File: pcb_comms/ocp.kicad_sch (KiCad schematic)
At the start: 10 parts, among them IC1 LDL1117S33R, IC2 TPS2553QDBVRQ1

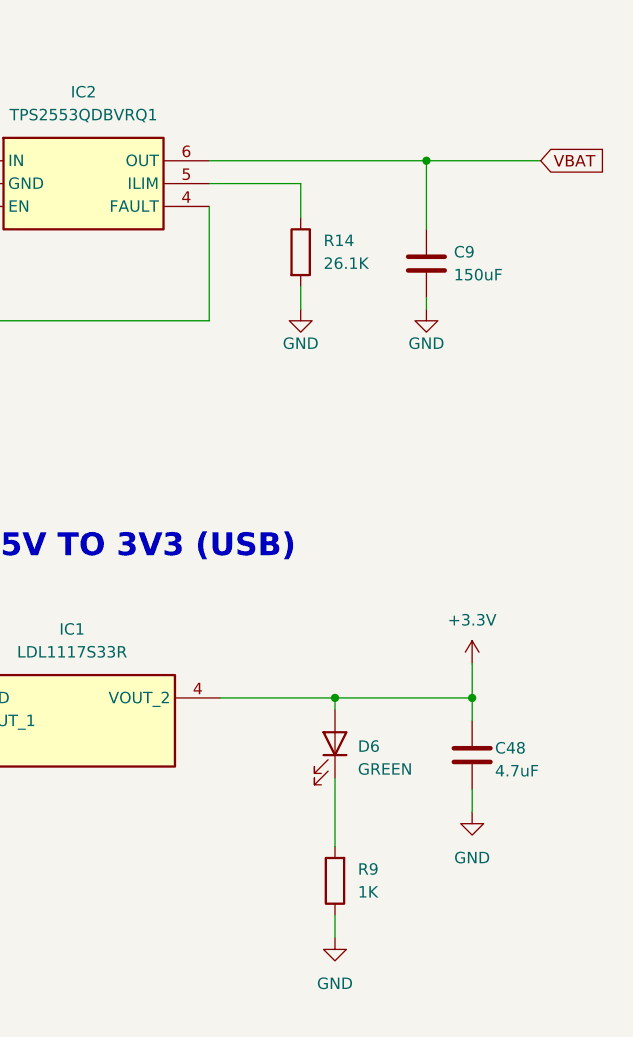
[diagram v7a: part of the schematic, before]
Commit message: Update schematic. Add net classes and JST footprints for aux
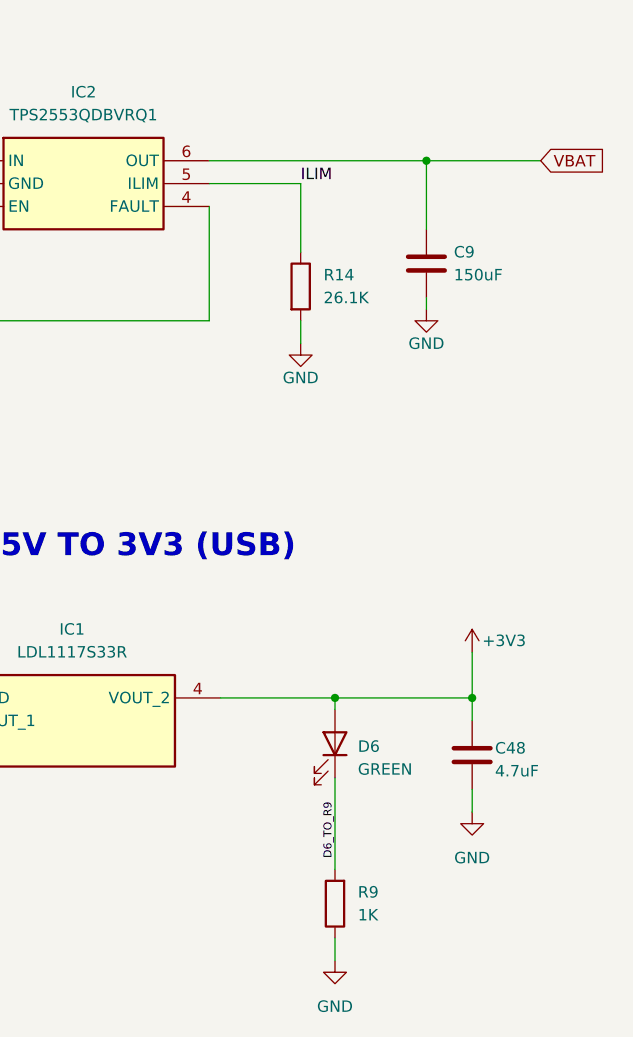
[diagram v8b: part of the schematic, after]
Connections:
- net D6_TO_R9: now reaches D6.1 (K), R9.2
- net ILIM: now reaches IC2.5 (ILIM), R14.1
- net +3.3V renamed +3V3
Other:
- moved on the sheet: R14, R9
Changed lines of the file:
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@@
+	)
+	(junction
+		(at 115.57 123.19)
+		(diameter 0)
+		(color 0 0 0 0)
+	)
+	(junction
+		(at 92.71 58.42)
+		(diameter 0)
+		(color 0 0 0 0)
 	)
 	(junction
@@
 	)
 	(junction
-		(at 115.57 123.19)
-		(diameter 0)
-		(color 0 0 0 0)
-	)
-	(junction
-		(at 92.71 58.42)
-		(diameter 0)
-		(color 0 0 0 0)
-	)
-	(junction
 		(at 184.15 58.42)
 		(diameter 0)
@@
 	(wire
 		(pts
-			(xy 173.99 127) (xy 173.99 134.62)
+			(xy 173.99 127) (xy 173.99 137.16)
 		)
 		(stroke
@@
 	(wire
 		(pts
-			(xy 170.18 72.39) (xy 170.18 74.93)
+			(xy 170.18 76.2) (xy 170.18 78.74)
+		)
+		(stroke
+			(width 0)
+			(type default)
+		)
+	)
+	(wire
+		(pts
+			(xy 189.23 113.03) (xy 189.23 118.11)
 		)
 		(stroke
@@
 	(wire
 		(pts
-			(xy 170.18 60.96) (xy 170.18 64.77)
+			(xy 170.18 60.96) (xy 170.18 68.58)
 		)
 		(stroke
@@
 	(wire
 		(pts
-			(xy 189.23 114.3) (xy 189.23 118.11)
-		)
-		(stroke
-			(width 0)
-			(type default)
-		)
-	)
-	(wire
-		(pts
 			(xy 173.99 118.11) (xy 189.23 118.11)
 		)
@@
 	(wire
 		(pts
-			(xy 173.99 142.24) (xy 173.99 144.78)
+			(xy 173.99 144.78) (xy 173.99 147.32)
 		)
 		(stroke
@@
 			(width 0)
 			(type default)
+		)
+	)
+	(label "D6_TO_R9"
+		(at 173.99 135.89 90)
+		(effects
+			(font
+				(size 0.889 0.889)
+			)
+			(justify left bottom)
+		)
+	)
+	(label "ILIM"
+		(at 170.18 60.96 0)
+		(effects
+			(font
+				(size 1.27 1.27)
+			)
+			(justify left bottom)
 		)
 	)
@@
 	(symbol
 		(lib_id "Device:R")
-		(at 173.99 138.43 180)
+		(at 173.99 140.97 180)
 		(unit 1)
 		(exclude_from_sim no)
@@
 		(fields_autoplaced yes)
 		(property "Reference" "R9"
-			(at 176.53 137.1599 0)
+			(at 176.53 139.6999 0)
 			(effects
 				(font
@@
 		)
 		(property "Value" "1K"
-			(at 176.53 139.6999 0)
+			(at 176.53 142.2399 0)
 			(effects
 				(font
@@
 		)
 		(property "Footprint" "Resistor_SMD:R_0805_2012Metric_Pad1.20x1.40mm_HandSolder"
-			(at 175.768 138.43 90)
+			(at 175.768 140.97 90)
 			(effects
 				(font
@@
 		)
 		(property "Datasheet" "~"
-			(at 173.99 138.43 0)
+			(at 173.99 140.97 0)
 			(effects
 				(font
@@
 		)
 		(property "Description" "Resistor"
-			(at 173.99 138.43 0)
+			(at 173.99 140.97 0)
 			(effects
 				(font
@@
 		)
 		(property "AVAILABILITY" ""
-			(at 173.99 138.43 0)
+			(at 173.99 140.97 0)
 			(effects
 				(font
@@
 		)
 		(property "DESCRIPTION" ""
-			(at 173.99 138.43 0)
+			(at 173.99 140.97 0)
 			(effects
 				(font
@@
 		)
 		(property "PACKAGE" ""
-			(at 173.99 138.43 0)
+			(at 173.99 140.97 0)
 			(effects
 				(font
@@
 		)
 		(property "PART_REV" ""
-			(at 173.99 138.43 0)
+			(at 173.99 140.97 0)
 			(effects
 				(font
@@
 		)
 		(property "PRICE" ""
-			(at 173.99 138.43 0)
+			(at 173.99 140.97 0)
 			(effects
 				(font
@@
 		)
 		(property "KLC_S3.3" ""
-			(at 173.99 138.43 0)
+			(at 173.99 140.97 0)
 			(effects
 				(font
@@
 		)
 		(property "KLC_S4.1" ""
-			(at 173.99 138.43 0)
+			(at 173.99 140.97 0)
 			(effects
 				(font
@@
 	)
 	(symbol
-		(lib_id "power:+3.3V")
-		(at 189.23 114.3 0)
-		(unit 1)
-		(exclude_from_sim no)
-		(in_bom yes)
-		(on_board yes)
-		(dnp no)
-		(property "Reference" "#PWR044"
-			(at 189.23 118.11 0)
-			(effects
-				(font
-					(size 1.27 1.27)
-				)
-				(hide yes)
-			)
-		)
-		(property "Value" "+3.3V"
-			(at 189.23 109.474 0)
-			(effects
-				(font
-					(size 1.27 1.27)
-				)
-			)
-		)
-		(property "Footprint" ""
-			(at 189.23 114.3 0)
-			(effects
-				(font
-					(size 1.27 1.27)
-				)
-				(hide yes)
-			)
-		)
-		(property "Datasheet" ""
-			(at 189.23 114.3 0)
-			(effects
-				(font
-					(size 1.27 1.27)
-				)
-				(hide yes)
-			)
-		)
-		(property "Description" "Power symbol creates a global label with name \"+3.3V\""
-			(at 189.23 114.3 0)
-			(effects
-				(font
-					(size 1.27 1.27)
-				)
-				(hide yes)
-			)
-		)
-		(pin "1"
-		)
-		(instances
-			(project "pcb_comms_board"
-				(path "/ea597178-b44d-4db9-826c-8f86e8d231f0/177e7153-e267-47bf-abd3-8b553807255e"
-					(reference "#PWR044")
-					(unit 1)
-				)
-			)
-		)
-	)
-	(symbol
 		(lib_id "Device:C")
 		(at 189.23 124.46 0)
@@
 	(symbol
 		(lib_id "power:GND")
-		(at 173.99 144.78 0)
+		(at 173.99 147.32 0)
 		(unit 1)
 		(exclude_from_sim no)
@@
 		(fields_autoplaced yes)
 		(property "Reference" "#PWR058"
-			(at 173.99 151.13 0)
+			(at 173.99 153.67 0)
 			(effects
 				(font
@@
 		)
 		(property "Value" "GND"
-			(at 173.99 149.86 0)
+			(at 173.99 152.4 0)
 			(effects
 				(font
@@
 		)
 		(property "Footprint" ""
-			(at 173.99 144.78 0)
+			(at 173.99 147.32 0)
 			(effects
 				(font
@@
 		)
 		(property "Datasheet" ""
-			(at 173.99 144.78 0)
+			(at 173.99 147.32 0)
 			(effects
 				(font
@@
 		)
 		(property "Description" "Power symbol creates a global label with name \"GND\" , ground"
-			(at 173.99 144.78 0)
+			(at 173.99 147.32 0)
 			(effects
 				(font
@@
 	(symbol
 		(lib_id "Device:R")
-		(at 170.18 68.58 0)
+		(at 170.18 72.39 0)
 		(unit 1)
 		(exclude_from_sim no)
@@
 		(fields_autoplaced yes)
 		(property "Reference" "R14"
-			(at 172.72 67.3099 0)
+			(at 172.72 71.1199 0)
 			(effects
 				(font
@@
 		)
 		(property "Value" "26.1K"
-			(at 172.72 69.8499 0)
+			(at 172.72 73.6599 0)
 			(effects
 				(font
@@
 		)
 		(property "Footprint" "Resistor_SMD:R_0805_2012Metric_Pad1.20x1.40mm_HandSolder"
-			(at 168.402 68.58 90)
+			(at 168.402 72.39 90)
 			(effects
 				(font
@@
 		)
 		(property "Datasheet" "~"
-			(at 170.18 68.58 0)
+			(at 170.18 72.39 0)
 			(effects
 				(font
@@
 		)
 		(property "Description" "Resistor"
-			(at 170.18 68.58 0)
+			(at 170.18 72.39 0)
 			(effects
 				(font
@@
 		)
 		(property "KLC_S3.3" ""
-			(at 170.18 68.58 0)
+			(at 170.18 72.39 0)
 			(effects
 				(font
@@
 		)
 		(property "KLC_S4.1" ""
-			(at 170.18 68.58 0)
+			(at 170.18 72.39 0)
 			(effects
 				(font
@@
 	(symbol
 		(lib_id "power:GND")
-		(at 170.18 74.93 0)
+		(at 170.18 78.74 0)
 		(unit 1)
 		(exclude_from_sim no)
@@
 		(dnp no)
 		(property "Reference" "#PWR020"
-			(at 170.18 81.28 0)
+			(at 170.18 85.09 0)
 			(effects
 				(font
@@
 		)
 		(property "Value" "GND"
+			(at 170.18 82.55 0)
+			(effects
+				(font
+					(size 1.27 1.27)
+				)
+			)
+		)
+		(property "Footprint" ""
 			(at 170.18 78.74 0)
 			(effects
@@
 					(size 1.27 1.27)
 				)
-			)
-		)
-		(property "Footprint" ""
-			(at 170.18 74.93 0)
-			(effects
-				(font
-					(size 1.27 1.27)
-				)
 				(hide yes)
 			)
 		)
 		(property "Datasheet" ""
-			(at 170.18 74.93 0)
+			(at 170.18 78.74 0)
 			(effects
 				(font
@@
 		)
 		(property "Description" "Power symbol creates a global label with name \"GND\" , ground"
-			(at 170.18 74.93 0)
+			(at 170.18 78.74 0)
 			(effects
 				(font
@@
 					(unit 1)
 				)
+			)
+		)
+	)
+	(symbol
+		(lib_id "power:+3V3")
+		(at 189.23 113.03 0)
+		(unit 1)
+		(exclude_from_sim no)
+		(in_bom yes)
+		(on_board yes)
+		(dnp no)
+		(property "Reference" "#PWR044"
+			(at 189.23 116.84 0)
+			(effects
+				(font
+					(size 1.27 1.27)
+				)
+				(hide yes)
+			)
+		)
+		(property "Value" "+3V3"
+			(at 192.786 111.76 0)
+			(effects
+				(font
+					(size 1.27 1.27)
+				)
+			)
+		)
+		(property "Footprint" ""
+			(at 189.23 113.03 0)
+			(effects
+				(font
+					(size 1.27 1.27)
+				)
+				(hide yes)
+			)
+		)
+		(property "Datasheet" ""
+			(at 189.23 113.03 0)
+			(effects
+				(font
+					(size 1.27 1.27)
+				)
+				(hide yes)
+			)
+		)
+		(property "Description" "Power symbol creates a global label with name \"+3V3\""
+			(at 189.23 113.03 0)
+			(effects
+				(font
+					(size 1.27 1.27)
+				)
+				(hide yes)
+			)
+		)
+		(pin "1"
+		)
+		(instances
+			(project "pcb_comms_board"
+				(path "/ea597178-b44d-4db9-826c-8f86e8d231f0/177e7153-e267-47bf-abd3-8b553807255e"
+					(reference "#PWR044")
+					(unit 1)
+				)
